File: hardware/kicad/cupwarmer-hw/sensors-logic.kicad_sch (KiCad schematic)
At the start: 7 parts, among them J1 I2C Service, J2 THERM_MON, J3 STATUS_MON

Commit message: Switch I2C/NTC pull-ups to RX_VAA and bump heater to 15R
- Pull-ups for SCL/SDA and NTC monitor nodes move from RX_VDD
  (1.1 V, too low for I2C) to RX_VAA (2.5 V).
- Heater value updated from 10 R to 15 R to keep dissipation
  within the EPP 15 W envelope after efficiency losses, avoiding
  VOUT droop and OCP trips.
- Design notes refreshed to reflect the DS14078 Figure 13 / Table 36
  alignment, ASK/ESD/Cd parts, and v1 fixed-on heater gate plan.
- Add untracked rx-power.kicad_pcb / rx-power.kicad_pro stubs.

Co-Authored-By: Claude Opus 4.7 (1M context) <noreply@anthropic.com>
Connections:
- net RX_VDD renamed RX_VAA
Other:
- note added: "TH1/TH2 are 10k NTC placeholders with 10k pull-up to RX_VAA so an external logger can read NTC_TOP / NTC_PCB directly"
- note removed: "TH1/TH2 are 10k NTC placeholders with 10k pull-up to RX_VDD so an external logger can read NTC_TOP / NTC_PCB directly"
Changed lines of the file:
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@@
 		)
 	)
-	(text "TH1/TH2 are 10k NTC placeholders with 10k pull-up to RX_VDD so an external logger can read NTC_TOP / NTC_PCB directly"
+	(text "TH1/TH2 are 10k NTC placeholders with 10k pull-up to RX_VAA so an external logger can read NTC_TOP / NTC_PCB directly"
 		(exclude_from_sim no)
 		(at 27.94 33.02 0)
@@
 		)
 	)
-	(global_label "RX_VDD"
+	(global_label "RX_VAA"
 		(shape passive)
 		(at 96.52 83.82 0)
@@
 		)
 	)
-	(global_label "RX_VDD"
+	(global_label "RX_VAA"
 		(shape passive)
 		(at 130.81 44.45 180)
@@
 			)
 		)
-		(property "Description" "RX_VDD pull-up for NTC_PCB monitor node"
+		(property "Description" "RX_VAA pull-up for NTC_PCB monitor node"
 			(at 81.28 99.06 0)
 			(hide yes)
@@
 			)
 		)
-		(property "Description" "Service header for STWLC38 bring-up with RX_VDD reference"
+		(property "Description" "Service header for STWLC38 bring-up with RX_VAA reference"
 			(at 142.24 48.26 0)
 			(hide yes)
@@
 			)
 		)
-		(property "Description" "RX_VDD pull-up for NTC_TOP monitor node"
+		(property "Description" "RX_VAA pull-up for NTC_TOP monitor node"
 			(at 81.28 88.9 0)
 			(hide yes)

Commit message: Tie TH2 to RX_NTC for STWLC38 internal OTP coverage
Move TH2 (10k NTC) from a standalone NTC_PCB net into the RX_NTC
divider so the STWLC38JRM internal OTP can read board/coil
hotspot temperature directly. R7 (10k -> RX_VAA, on rx-power
sheet) now forms the upper half of the divider with TH2 as the
lower half (~RX_VAA/2 at 25C); the redundant R9 pull-up on
sensors-logic is removed. NTC_TOP (TH1) keeps its existing
RX_VAA/R8 pull-up and J2 monitor tap since the IC has only one
NTC pin.

TH2 should be placed near the Qi coil/ferrite during layout so
the IC can autonomously throttle/stop on coil overheat -- a
second autonomous protection layer alongside the F1 thermostat.

Updates sensors-logic.kicad_sch (label rename, R9 + wire/junction
removal, J2 retap to RX_NTC, annotation), rx-power.kicad_sch
(R7 description), hardware/bom/initial-bom.csv (NTC_B + R7 notes),
and docs/design-notes.md (control/protection sections, schematic
status, mermaid block diagram). ERC: 0 violations.

Co-Authored-By: Claude Opus 4.7 (1M context) <noreply@anthropic.com>
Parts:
- removed R9: 10k Pull-up, symbol cupwarmer:PASSIVE_2
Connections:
- net NTC_PCB renamed RX_NTC
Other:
- note added: "TH1 (NTC_TOP) is 10k NTC + 10k pull-up to RX_VAA for external logger; TH2 ties to RX_NTC for STWLC38 internal OTP (place TH2 near Qi coil)"
- note removed: "TH1/TH2 are 10k NTC placeholders with 10k pull-up to RX_VAA so an external logger can read NTC_TOP / NTC_PCB directly"
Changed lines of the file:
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@@
 		)
 	)
-	(text "TH1/TH2 are 10k NTC placeholders with 10k pull-up to RX_VAA so an external logger can read NTC_TOP / NTC_PCB directly"
+	(text "TH1 (NTC_TOP) is 10k NTC + 10k pull-up to RX_VAA for external logger; TH2 ties to RX_NTC for STWLC38 internal OTP (place TH2 near Qi coil)"
 		(exclude_from_sim no)
 		(at 27.94 33.02 0)
@@
 	(wire
 		(pts
-			(xy 86.36 99.06) (xy 91.44 99.06)
-		)
-		(stroke
-			(width 0)
-			(type solid)
-		)
-	)
-	(wire
-		(pts
 			(xy 86.36 88.9) (xy 91.44 88.9)
 		)
@@
 	(wire
 		(pts
-			(xy 91.44 83.82) (xy 91.44 99.06)
+			(xy 91.44 83.82) (xy 91.44 88.9)
 		)
 		(stroke
@@
 	(wire
 		(pts
-			(xy 66.04 99.06) (xy 76.2 99.06)
+			(xy 66.04 99.06) (xy 73.66 99.06)
 		)
 		(stroke
@@
 		)
 	)
-	(global_label "NTC_PCB"
+	(global_label "RX_NTC"
 		(shape passive)
 		(at 149.86 88.9 0)
@@
 		)
 	)
-	(global_label "NTC_PCB"
+	(global_label "RX_NTC"
 		(shape passive)
 		(at 68.58 106.68 180)
@@
 	)
 	(symbol
-		(lib_id "cupwarmer:PASSIVE_2")
-		(at 81.28 99.06 0)
-		(unit 1)
-		(body_style 1)
-		(exclude_from_sim no)
-		(in_bom yes)
-		(on_board yes)
-		(in_pos_files yes)
-		(dnp no)
-		(property "Reference" "R9"
-			(at 81.28 102.87 0)
-			(show_name no)
-			(do_not_autoplace no)
-			(effects
-				(font
-					(size 1.27 1.27)
-				)
-			)
-		)
-		(property "Value" "10k Pull-up"
-			(at 81.28 95.25 0)
-			(show_name no)
-			(do_not_autoplace no)
-			(effects
-				(font
-					(size 1.27 1.27)
-				)
-			)
-		)
-		(property "Footprint" ""
-			(at 81.28 99.06 0)
-			(hide yes)
-			(show_name no)
-			(do_not_autoplace no)
-			(effects
-				(font
-					(size 1.27 1.27)
-				)
-			)
-		)
-		(property "Datasheet" "~"
-			(at 81.28 99.06 0)
-			(hide yes)
-			(show_name no)
-			(do_not_autoplace no)
-			(effects
-				(font
-					(size 1.27 1.27)
-				)
-			)
-		)
-		(property "Description" "RX_VAA pull-up for NTC_PCB monitor node"
-			(at 81.28 99.06 0)
-			(hide yes)
-			(show_name no)
-			(do_not_autoplace no)
-			(effects
-				(font
-					(size 1.27 1.27)
-				)
-			)
-		)
-		(pin "1"
-		)
-		(pin "2"
-		)
-		(instances
-			(project "cupwarmer-hw"
-				(path "/f3c63676-f392-4700-9f58-a6787e1eb284/33333333-3333-3333-3333-333333333333"
-					(reference "R9")
-					(unit 1)
-				)
-			)
-		)
-	)
-	(symbol
 		(lib_id "cupwarmer:DEBUG_HDR_4")
 		(at 142.24 48.26 0)
@@
 			)
 		)
-		(property "Description" "Bring-up header for NTC_TOP and NTC_PCB monitor nodes"
+		(property "Description" "Bring-up header for NTC_TOP and RX_NTC monitor taps"
 			(at 142.24 88.9 0)
 			(hide yes)

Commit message: Manual cleanup pass on rx-power and sensors-logic sheets
Co-Authored-By: Claude Opus 4.7 (1M context) <noreply@anthropic.com>
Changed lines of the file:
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@@
-	)
-	(junction
-		(at 91.44 88.9)
-		(diameter 0)
-		(color 0 0 0 0)
 	)
 	(junction
 		(at 73.66 88.9)
-		(diameter 0)
-		(color 0 0 0 0)
-	)
-	(junction
-		(at 73.66 99.06)
 		(diameter 0)
 		(color 0 0 0 0)
@@
 	(wire
 		(pts
+			(xy 91.44 83.82) (xy 96.52 83.82)
+		)
+		(stroke
+			(width 0)
+			(type solid)
+		)
+	)
+	(wire
+		(pts
 			(xy 50.8 99.06) (xy 55.88 99.06)
 		)
@@
 		(pts
 			(xy 66.04 99.06) (xy 73.66 99.06)
+		)
+		(stroke
+			(width 0)
+			(type solid)
+		)
+	)
+	(wire
+		(pts
+			(xy 73.66 99.06) (xy 73.66 106.68)
+		)
+		(stroke
+			(width 0)
+			(type solid)
+		)
+	)
+	(wire
+		(pts
+			(xy 68.58 106.68) (xy 73.66 106.68)
 		)
 		(stroke
@@
 	(wire
 		(pts
-			(xy 73.66 99.06) (xy 73.66 106.68)
-		)
-		(stroke
-			(width 0)
-			(type solid)
-		)
-	)
-	(wire
-		(pts
-			(xy 91.44 83.82) (xy 96.52 83.82)
-		)
-		(stroke
-			(width 0)
-			(type solid)
-		)
-	)
-	(wire
-		(pts
 			(xy 68.58 81.28) (xy 73.66 81.28)
 		)
 		(stroke
-			(width 0)
-			(type solid)
-		)
-	)
-	(wire
-		(pts
-			(xy 68.58 106.68) (xy 73.66 106.68)
-		)
-		(stroke

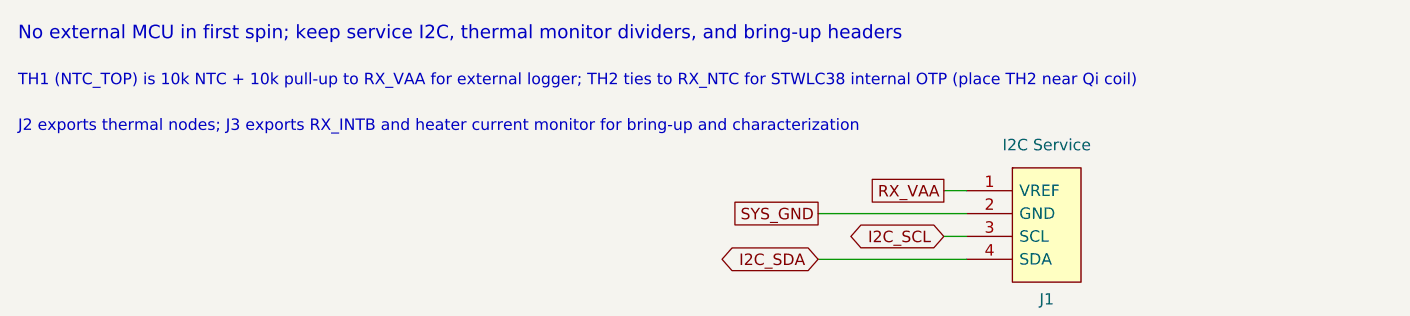
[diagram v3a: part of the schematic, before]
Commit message: Update design notes and sheet annotations for v1 decisions
- design-notes: record cup contact layer choice (alumina-filled silicone
  pad) and close out LED-2/INTB indicator decision (D2 driven from
  RX_VAA -> R11 -> GPIO0; INTB exposed via J3 only, no LED driver)
- cupwarmer-hw root sheet: refresh key global labels annotation
- sensors-logic: reword "first spin" -> "v1" for consistency
- rx-power: nudge R10 down 1.27mm to clear surrounding labels

Co-Authored-By: Claude Opus 4.7 (1M context) <noreply@anthropic.com>
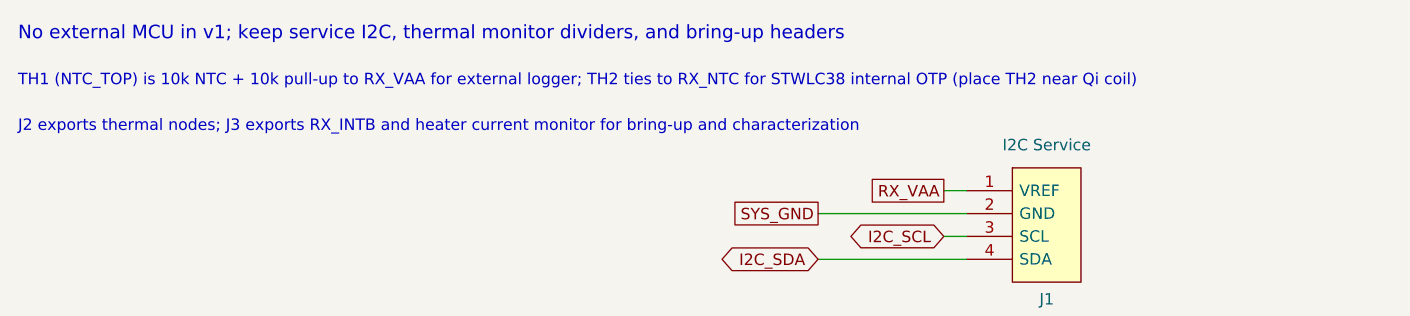
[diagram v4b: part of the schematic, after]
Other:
- note added: "No external MCU in v1; keep service I2C, thermal monitor dividers, and bring-up headers"
- note removed: "No external MCU in first spin; keep service I2C, thermal monitor dividers, and bring-up headers"
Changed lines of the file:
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@@
 		(comment 2 "Service, monitor, and thermal sensing")
 	)
-	(text "No external MCU in first spin; keep service I2C, thermal monitor dividers, and bring-up headers"
+	(text "No external MCU in v1; keep service I2C, thermal monitor dividers, and bring-up headers"
 		(exclude_from_sim no)
 		(at 27.94 27.94 0)
